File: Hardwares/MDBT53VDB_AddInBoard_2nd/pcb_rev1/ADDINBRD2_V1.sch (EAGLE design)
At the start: 8 parts, among them Q1 DMP2035UFDF-7, Q2 BC817-40QA, SW1 SKRPACE010, U1 SN74AHC1G00DRLR

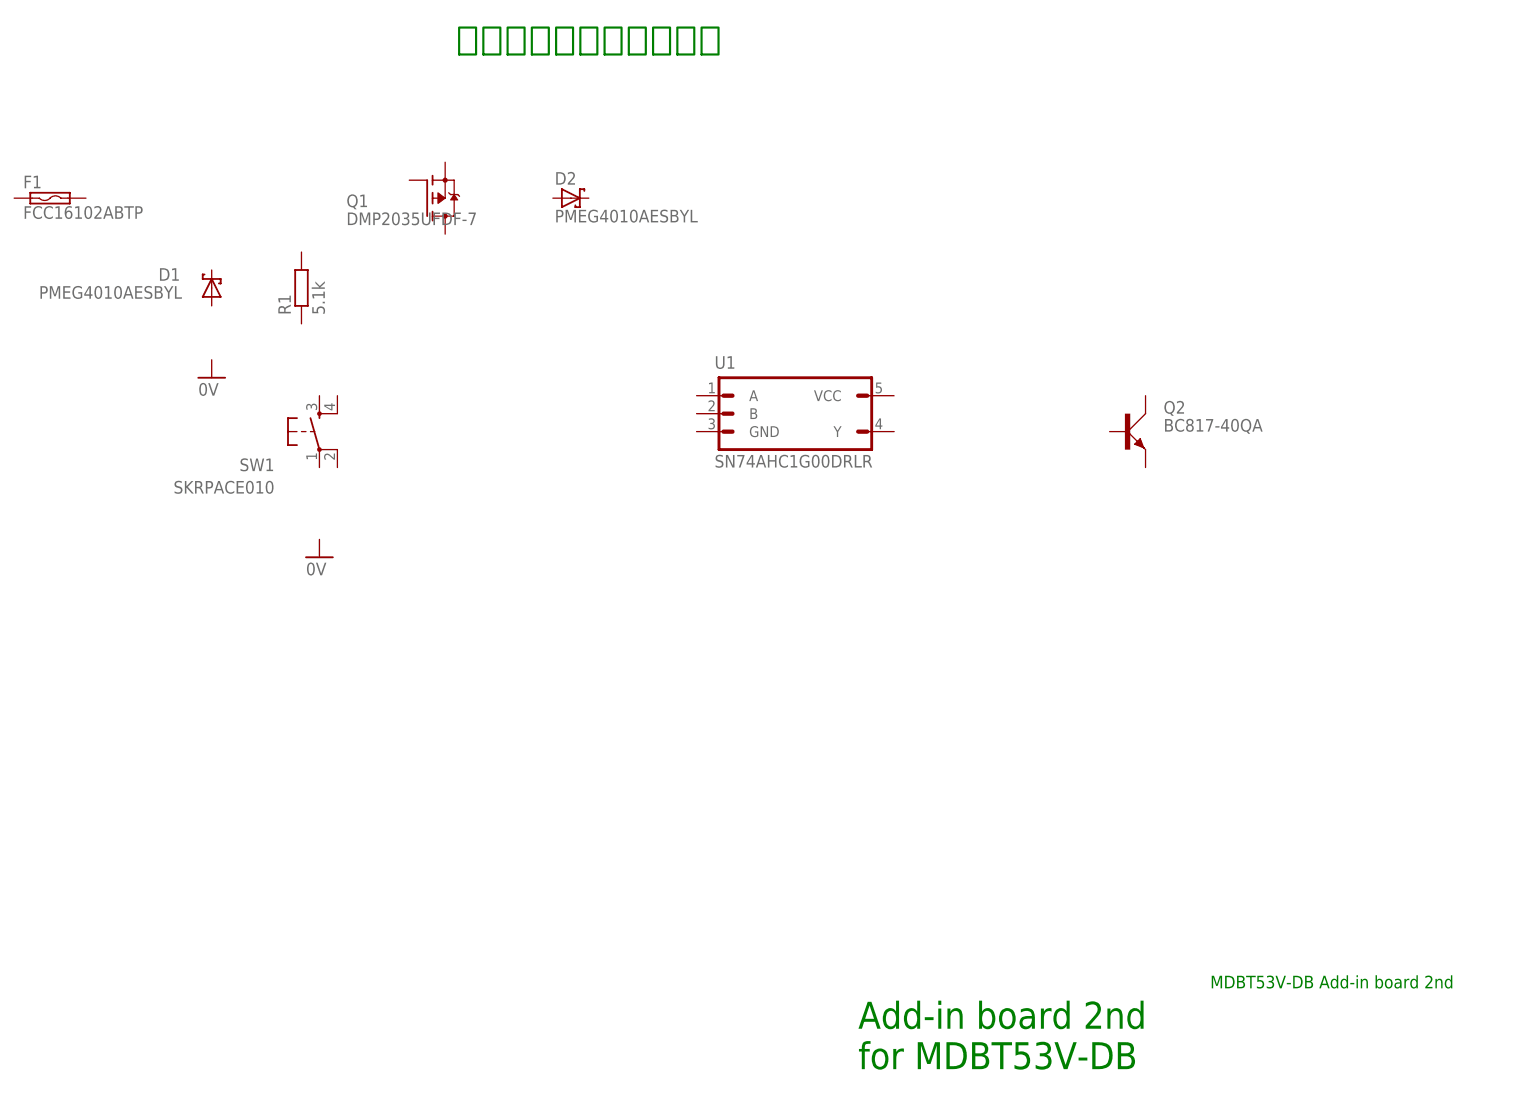
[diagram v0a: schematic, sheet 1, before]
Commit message: 回路図を修正
・電源投入／遮断回路の配線
・抵抗器２点を追加
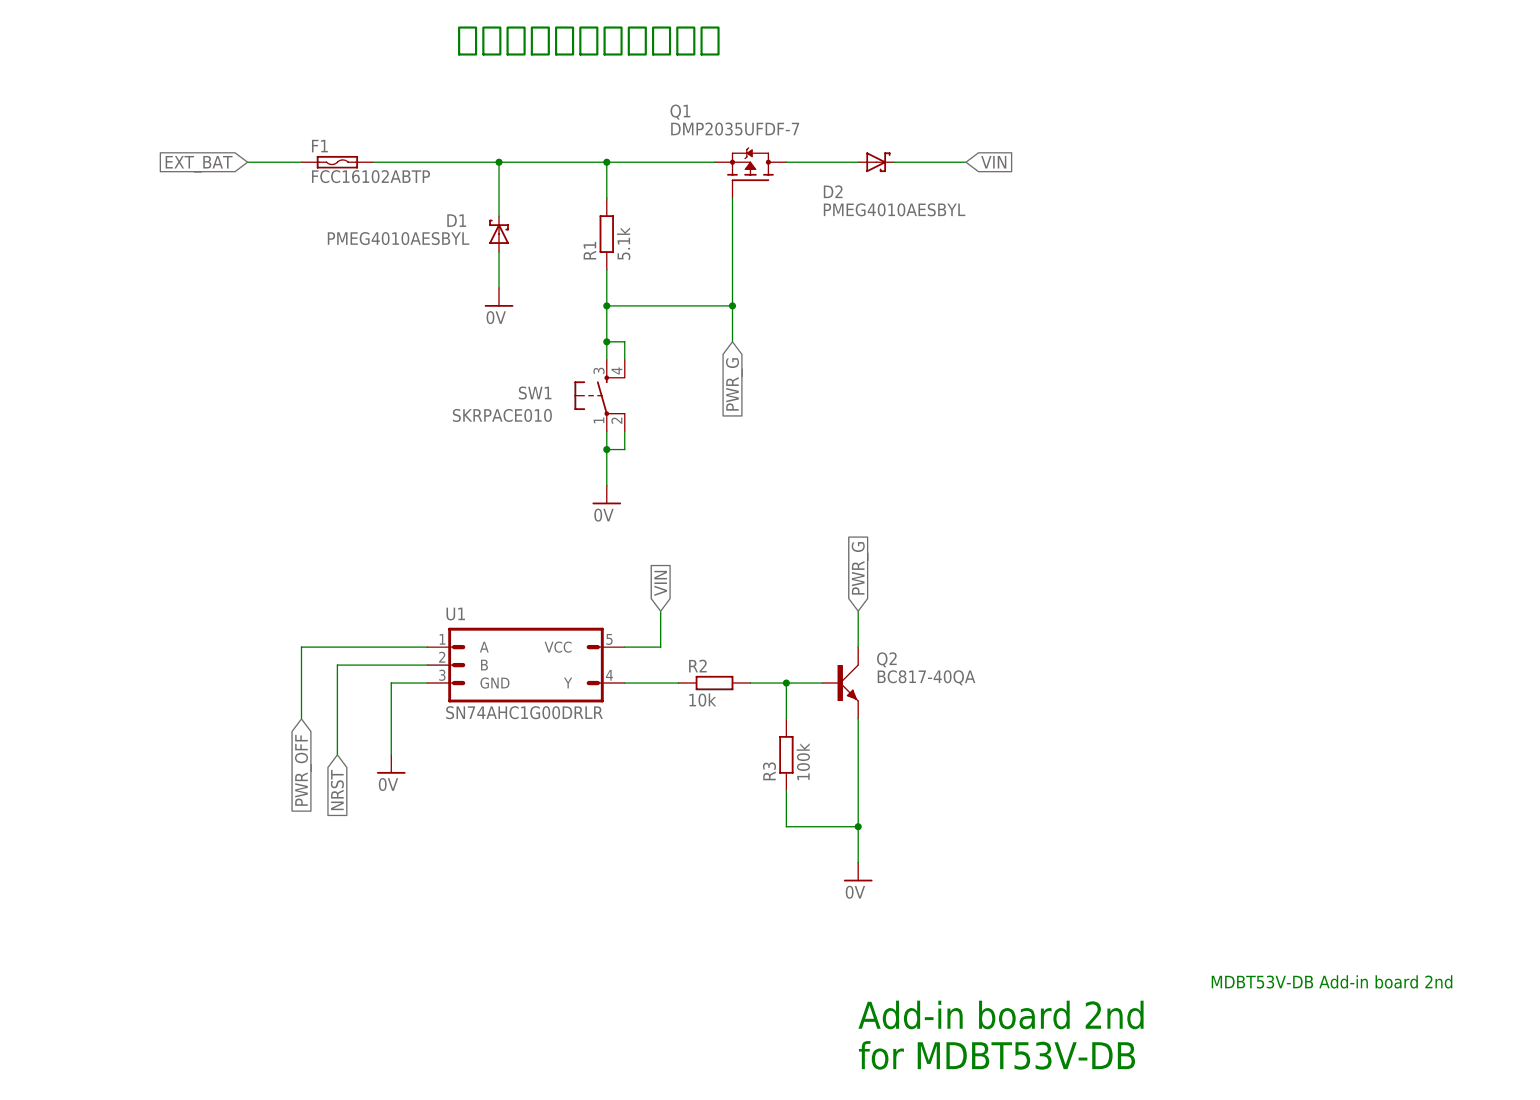
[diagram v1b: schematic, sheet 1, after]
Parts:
- added R2: 10k, Parts:RESISTOR_0402N
- added R3: 100k, Parts:RESISTOR_0402N
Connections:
- new net 0V: D1.A, Q2.E, R3.1, SW1.P, SW1.P1, U1.GND
- new net EXT_BAT: F1.1
- new net N$1: D1.C, F1.2, Q1.S, R1.2
- new net N$2: R2.1, U1.Y
- new net N$4: D2.A, Q1.D
- new net N$5: Q2.B, R2.2, R3.2
- new net NRST: U1.B
- new net PWR_G: Q1.G, Q2.C, R1.1, SW1.S, SW1.S1
- new net PWR_OFF: U1.A
- new net VIN: D2.C, U1.VCC
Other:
- moved on the sheet: D1, D2, F1, Q1, Q2, R1, SW1, U1
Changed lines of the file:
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@@
 <part name="U1" library="Parts" deviceset="SN74AHC1G00" device="DRLR"/>
 <part name="Q2" library="Parts" deviceset="BC817" device="-40QA"/>
+<part name="GND3" library="Supply" deviceset="0V" device=""/>
+<part name="R2" library="Parts" deviceset="RESISTOR" device="_0402N" value="10k"/>
+<part name="R3" library="Parts" deviceset="RESISTOR" device="_0402N" value="100k"/>
+<part name="GND4" library="Supply" deviceset="0V" device=""/>
 </parts>
 <sheets>
@@
 <instances>
 <instance part="FRAME1" gate="G$1" x="0" y="0"/>
-<instance part="F1" gate="G$1" x="53.34" y="132.08"/>
-<instance part="D1" gate="G$1" x="76.2" y="119.38" smashed="yes" rot="R90">
-<attribute name="NAME" x="71.755" y="122.174" size="1.778" layer="95" rot="R180"/>
-<attribute name="VALUE" x="72.009" y="119.634" size="1.778" layer="96" rot="R180"/>
+<instance part="F1" gate="G$1" x="93.98" y="137.16"/>
+<instance part="D1" gate="G$1" x="116.84" y="127" smashed="yes" rot="R90">
+<attribute name="NAME" x="112.395" y="129.794" size="1.778" layer="95" rot="R180"/>
+<attribute name="VALUE" x="112.649" y="127.254" size="1.778" layer="96" rot="R180"/>
 </instance>
-<instance part="SW1" gate="G$1" x="91.44" y="99.06" smashed="yes">
-<attribute name="NAME" x="85.09" y="95.25" size="1.778" layer="95" rot="R180"/>
-<attribute name="VALUE" x="85.09" y="92.075" size="1.778" layer="96" rot="R180"/>
+<instance part="SW1" gate="G$1" x="132.08" y="104.14" smashed="yes">
+<attribute name="NAME" x="124.46" y="105.41" size="1.778" layer="95" rot="R180"/>
+<attribute name="VALUE" x="124.46" y="102.235" size="1.778" layer="96" rot="R180"/>
 </instance>
-<instance part="GND1" gate="1" x="76.2" y="106.68"/>
-<instance part="GND2" gate="1" x="91.44" y="81.28"/>
-<instance part="R1" gate="G$1" x="88.9" y="114.3" rot="R90"/>
-<instance part="D2" gate="G$1" x="127" y="132.08"/>
-<instance part="Q1" gate="G$1" x="106.68" y="132.08"/>
-<instance part="U1" gate="G$1" x="144.78" y="104.14"/>
-<instance part="Q2" gate="G$1" x="203.2" y="99.06"/>
+<instance part="GND1" gate="1" x="116.84" y="116.84"/>
+<instance part="GND2" gate="1" x="132.08" y="88.9"/>
+<instance part="R1" gate="G$1" x="132.08" y="121.92" rot="R90"/>
+<instance part="D2" gate="G$1" x="170.18" y="137.16" smashed="yes">
+<attribute name="NAME" x="162.56" y="132.08" size="1.778" layer="95"/>
+<attribute name="VALUE" x="162.56" y="129.54" size="1.778" layer="96"/>
+</instance>
+<instance part="Q1" gate="G$1" x="152.4" y="134.62" smashed="yes" rot="R90">
+<attribute name="VALUE" x="140.97" y="140.97" size="1.778" layer="96"/>
+<attribute name="NAME" x="140.97" y="143.51" size="1.778" layer="95"/>
+</instance>
+<instance part="U1" gate="G$1" x="106.68" y="68.58"/>
+<instance part="Q2" gate="G$1" x="162.56" y="63.5"/>
+<instance part="GND3" gate="1" x="101.6" y="50.8"/>
+<instance part="R2" gate="G$1" x="142.24" y="63.5"/>
+<instance part="R3" gate="G$1" x="157.48" y="48.26" rot="R90"/>
+<instance part="GND4" gate="1" x="167.64" y="35.56"/>
 </instances>
 <busses>
 </busses>
 <nets>
+<net name="N$1" class="0">
+<segment>
+<pinref part="F1" gate="G$1" pin="2"/>
+<wire x1="99.06" y1="137.16" x2="116.84" y2="137.16" width="0.1524" layer="91"/>
+<pinref part="R1" gate="G$1" pin="2"/>
+<wire x1="116.84" y1="137.16" x2="132.08" y2="137.16" width="0.1524" layer="91"/>
+<wire x1="132.08" y1="137.16" x2="132.08" y2="132.08" width="0.1524" layer="91"/>
+<pinref part="D1" gate="G$1" pin="C"/>
+<wire x1="116.84" y1="137.16" x2="116.84" y2="129.54" width="0.1524" layer="91"/>
+<junction x="116.84" y="137.16"/>
+<junction x="132.08" y="137.16"/>
+<pinref part="Q1" gate="G$1" pin="S"/>
+<wire x1="132.08" y1="137.16" x2="147.32" y2="137.16" width="0.1524" layer="91"/>
+</segment>
+</net>
+<net name="0V" class="0">
+<segment>
+<pinref part="D1" gate="G$1" pin="A"/>
+<pinref part="GND1" gate="1" pin="0V"/>
+<wire x1="116.84" y1="124.46" x2="116.84" y2="119.38" width="0.1524" layer="91"/>
+</segment>
+<segment>
+<pinref part="SW1" gate="G$1" pin="P"/>
+<pinref part="GND2" gate="1" pin="0V"/>
+<wire x1="132.08" y1="99.06" x2="132.08" y2="96.52" width="0.1524" layer="91"/>
+<pinref part="SW1" gate="G$1" pin="P1"/>
+<wire x1="132.08" y1="96.52" x2="132.08" y2="91.44" width="0.1524" layer="91"/>
+<wire x1="134.62" y1="99.06" x2="134.62" y2="96.52" width="0.1524" layer="91"/>
+<wire x1="134.62" y1="96.52" x2="132.08" y2="96.52" width="0.1524" layer="91"/>
+<junction x="132.08" y="96.52"/>
+</segment>
+<segment>
+<pinref part="U1" gate="G$1" pin="GND"/>
+<wire x1="106.68" y1="63.5" x2="101.6" y2="63.5" width="0.1524" layer="91"/>
+<pinref part="GND3" gate="1" pin="0V"/>
+<wire x1="101.6" y1="53.34" x2="101.6" y2="63.5" width="0.1524" layer="91"/>
+</segment>
+<segment>
+<pinref part="Q2" gate="G$1" pin="E"/>
+<pinref part="GND4" gate="1" pin="0V"/>
+<wire x1="167.64" y1="58.42" x2="167.64" y2="43.18" width="0.1524" layer="91"/>
+<pinref part="R3" gate="G$1" pin="1"/>
+<wire x1="167.64" y1="43.18" x2="167.64" y2="38.1" width="0.1524" layer="91"/>
+<wire x1="157.48" y1="48.26" x2="157.48" y2="43.18" width="0.1524" layer="91"/>
+<wire x1="157.48" y1="43.18" x2="167.64" y2="43.18" width="0.1524" layer="91"/>
+<junction x="167.64" y="43.18"/>
+</segment>
+</net>
+<net name="PWR_G" class="0">
+<segment>
+<pinref part="R1" gate="G$1" pin="1"/>
+<pinref part="SW1" gate="G$1" pin="S"/>
+<wire x1="132.08" y1="121.92" x2="132.08" y2="116.84" width="0.1524" layer="91"/>
+<pinref part="SW1" gate="G$1" pin="S1"/>
+<wire x1="132.08" y1="116.84" x2="132.08" y2="111.76" width="0.1524" layer="91"/>
+<wire x1="132.08" y1="111.76" x2="132.08" y2="109.22" width="0.1524" layer="91"/>
+<wire x1="132.08" y1="111.76" x2="134.62" y2="111.76" width="0.1524" layer="91"/>
+<wire x1="134.62" y1="111.76" x2="134.62" y2="109.22" width="0.1524" layer="91"/>
+<junction x="132.08" y="116.84"/>
+<wire x1="132.08" y1="116.84" x2="149.86" y2="116.84" width="0.1524" layer="91"/>
+<pinref part="Q1" gate="G$1" pin="G"/>
+<wire x1="149.86" y1="132.08" x2="149.86" y2="116.84" width="0.1524" layer="91"/>
+<wire x1="149.86" y1="116.84" x2="149.86" y2="111.76" width="0.1524" layer="91"/>
+<label x="149.86" y="111.76" size="1.778" layer="95" rot="R270" xref="yes"/>
+<junction x="149.86" y="116.84"/>
+<junction x="132.08" y="111.76"/>
+</segment>
+<segment>
+<pinref part="Q2" gate="G$1" pin="C"/>
+<wire x1="167.64" y1="68.58" x2="167.64" y2="73.66" width="0.1524" layer="91"/>
+<label x="167.64" y="73.66" size="1.778" layer="95" rot="R90" xref="yes"/>
+</segment>
+</net>
+<net name="N$4" class="0">
+<segment>
+<pinref part="Q1" gate="G$1" pin="D"/>
+<pinref part="D2" gate="G$1" pin="A"/>
+<wire x1="157.48" y1="137.16" x2="167.64" y2="137.16" width="0.1524" layer="91"/>
+</segment>
+</net>
+<net name="VIN" class="0">
+<segment>
+<pinref part="D2" gate="G$1" pin="C"/>
+<wire x1="172.72" y1="137.16" x2="182.88" y2="137.16" width="0.1524" layer="91"/>
+<label x="182.88" y="137.16" size="1.778" layer="95" xref="yes"/>
+</segment>
+<segment>
+<pinref part="U1" gate="G$1" pin="VCC"/>
+<wire x1="134.62" y1="68.58" x2="139.7" y2="68.58" width="0.1524" layer="91"/>
+<wire x1="139.7" y1="68.58" x2="139.7" y2="73.66" width="0.1524" layer="91"/>
+<label x="139.7" y="73.66" size="1.778" layer="95" rot="R90" xref="yes"/>
+</segment>
+</net>
+<net name="EXT_BAT" class="0">
+<segment>
+<pinref part="F1" gate="G$1" pin="1"/>
+<wire x1="88.9" y1="137.16" x2="81.28" y2="137.16" width="0.1524" layer="91"/>
+<label x="81.28" y="137.16" size="1.778" layer="95" rot="R180" xref="yes"/>
+</segment>
+</net>
+<net name="PWR_OFF" class="0">
+<segment>
+<pinref part="U1" gate="G$1" pin="A"/>
+<wire x1="106.68" y1="68.58" x2="88.9" y2="68.58" width="0.1524" layer="91"/>
+<wire x1="88.9" y1="68.58" x2="88.9" y2="58.42" width="0.1524" layer="91"/>
+<label x="88.9" y="58.42" size="1.778" layer="95" rot="R270" xref="yes"/>
+</segment>
+</net>
+<net name="NRST" class="0">
+<segment>
+<pinref part="U1" gate="G$1" pin="B"/>
+<wire x1="106.68" y1="66.04" x2="93.98" y2="66.04" width="0.1524" layer="91"/>
+<wire x1="93.98" y1="66.04" x2="93.98" y2="53.34" width="0.1524" layer="91"/>
+<label x="93.98" y="53.34" size="1.778" layer="95" rot="R270" xref="yes"/>
+</segment>
+</net>
+<net name="N$2" class="0">
+<segment>
+<pinref part="U1" gate="G$1" pin="Y"/>
+<pinref part="R2" gate="G$1" pin="1"/>
+<wire x1="134.62" y1="63.5" x2="142.24" y2="63.5" width="0.1524" layer="91"/>
+</segment>
+</net>
+<net name="N$5" class="0">
+<segment>
+<pinref part="R2" gate="G$1" pin="2"/>
+<pinref part="Q2" gate="G$1" pin="B"/>
+<wire x1="152.4" y1="63.5" x2="157.48" y2="63.5" width="0.1524" layer="91"/>
+<pinref part="R3" gate="G$1" pin="2"/>
+<wire x1="157.48" y1="63.5" x2="162.56" y2="63.5" width="0.1524" layer="91"/>
+<wire x1="157.48" y1="58.42" x2="157.48" y2="63.5" width="0.1524" layer="91"/>
+<junction x="157.48" y="63.5"/>
+</segment>
+</net>
 </nets>
 </sheet>

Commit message: 回路図を修正
・ベース抵抗の定数を変更
・コメントを追加
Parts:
- R2: value 10k -> 5.1k
- R3: value 100k -> 51k
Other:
- note added: "動作電源投入： タクトスイッチを約１秒間押し続けると VINに電源が供給されます。"
- note added: "動作電源遮断： PWR_OFFにHIGHを入力すると、 PWR_Gが閉塞され、VINに電源が 供給されなくなります。"
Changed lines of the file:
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@@
 <part name="Q2" library="Parts" deviceset="BC817" device="-40QA"/>
 <part name="GND3" library="Supply" deviceset="0V" device=""/>
-<part name="R2" library="Parts" deviceset="RESISTOR" device="_0402N" value="10k"/>
-<part name="R3" library="Parts" deviceset="RESISTOR" device="_0402N" value="100k"/>
+<part name="R2" library="Parts" deviceset="RESISTOR" device="_0402N" value="5.1k"/>
+<part name="R3" library="Parts" deviceset="RESISTOR" device="_0402N" value="51k"/>
 <part name="GND4" library="Supply" deviceset="0V" device=""/>
 </parts>
@@
 for MDBT53V-DB</text>
 <text x="129.54" y="152.4" size="3.81" layer="91" align="bottom-center">動作電源投入・遮断回路</text>
+<text x="78.74" y="99.06" size="1.778" layer="91" align="top-left">動作電源投入：
+タクトスイッチを約１秒間押し続けると
+VINに電源が供給されます。</text>
+<text x="78.74" y="40.64" size="1.778" layer="91" align="top-left">動作電源遮断：
+PWR_OFFにHIGHを入力すると、
+PWR_Gが閉塞され、VINに電源が
+供給されなくなります。</text>
 </plain>
 <instances>

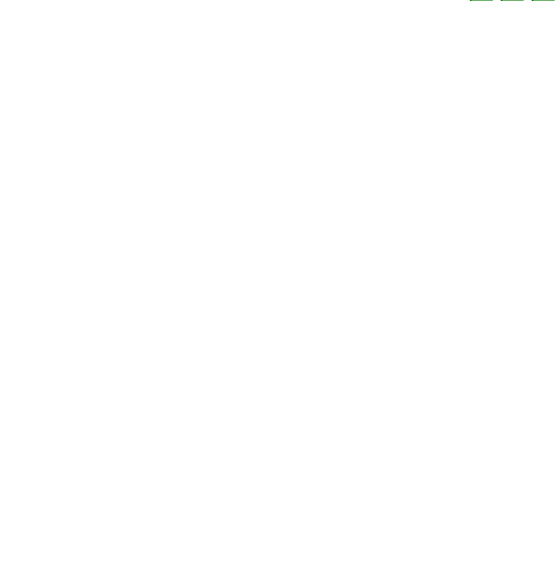
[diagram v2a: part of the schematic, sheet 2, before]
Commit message: 回路図を修正
・基準電圧ICを配置
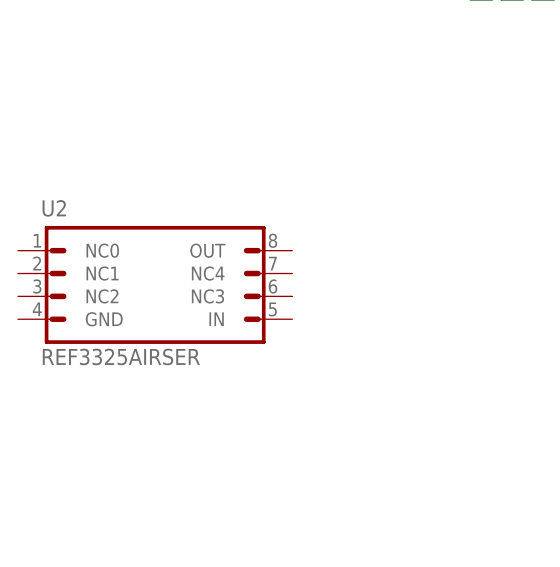
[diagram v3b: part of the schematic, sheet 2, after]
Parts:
- added U2: REF3325AIRSER, ICs:REF3325AIRSER
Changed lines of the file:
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@@
 <part name="R3" library="Parts" deviceset="RESISTOR" device="_0402N" value="51k"/>
 <part name="GND4" library="Supply" deviceset="0V" device=""/>
+<part name="U2" library="ICs" deviceset="REF33" device="25AIRSER"/>
 </parts>
 <sheets>
@@
 <instances>
 <instance part="FRAME2" gate="G$1" x="0" y="0"/>
+<instance part="U2" gate="G$1" x="81.28" y="119.38"/>
 </instances>
 <busses>
